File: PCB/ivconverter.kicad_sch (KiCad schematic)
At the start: 9 parts, among them U3 OPA1612AxD

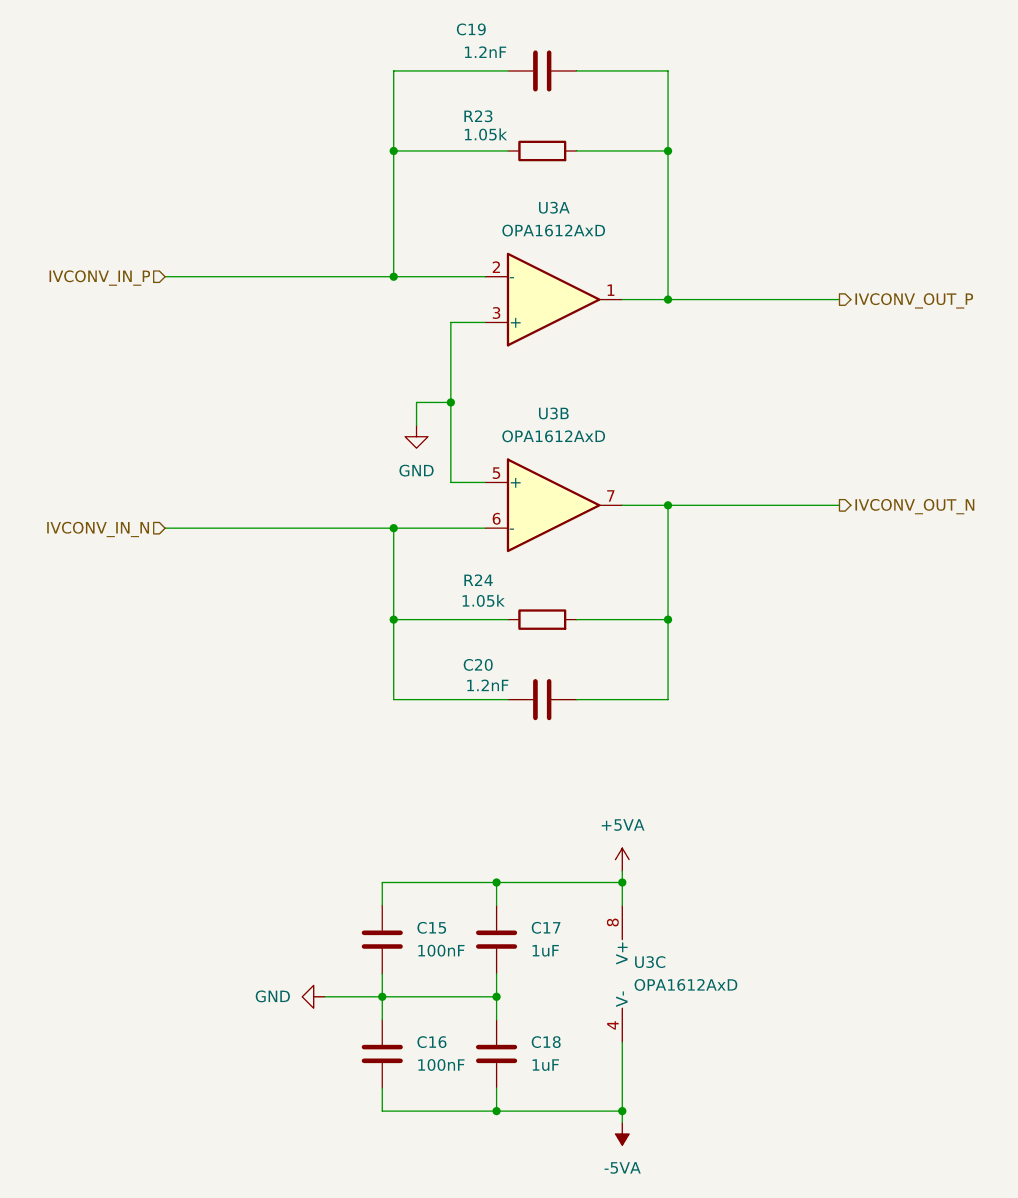
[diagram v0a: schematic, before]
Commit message: Changed single ended connector for gold plated part and changed resistor and capacitor values of opa1622 amp for improved power on high impedance headphones
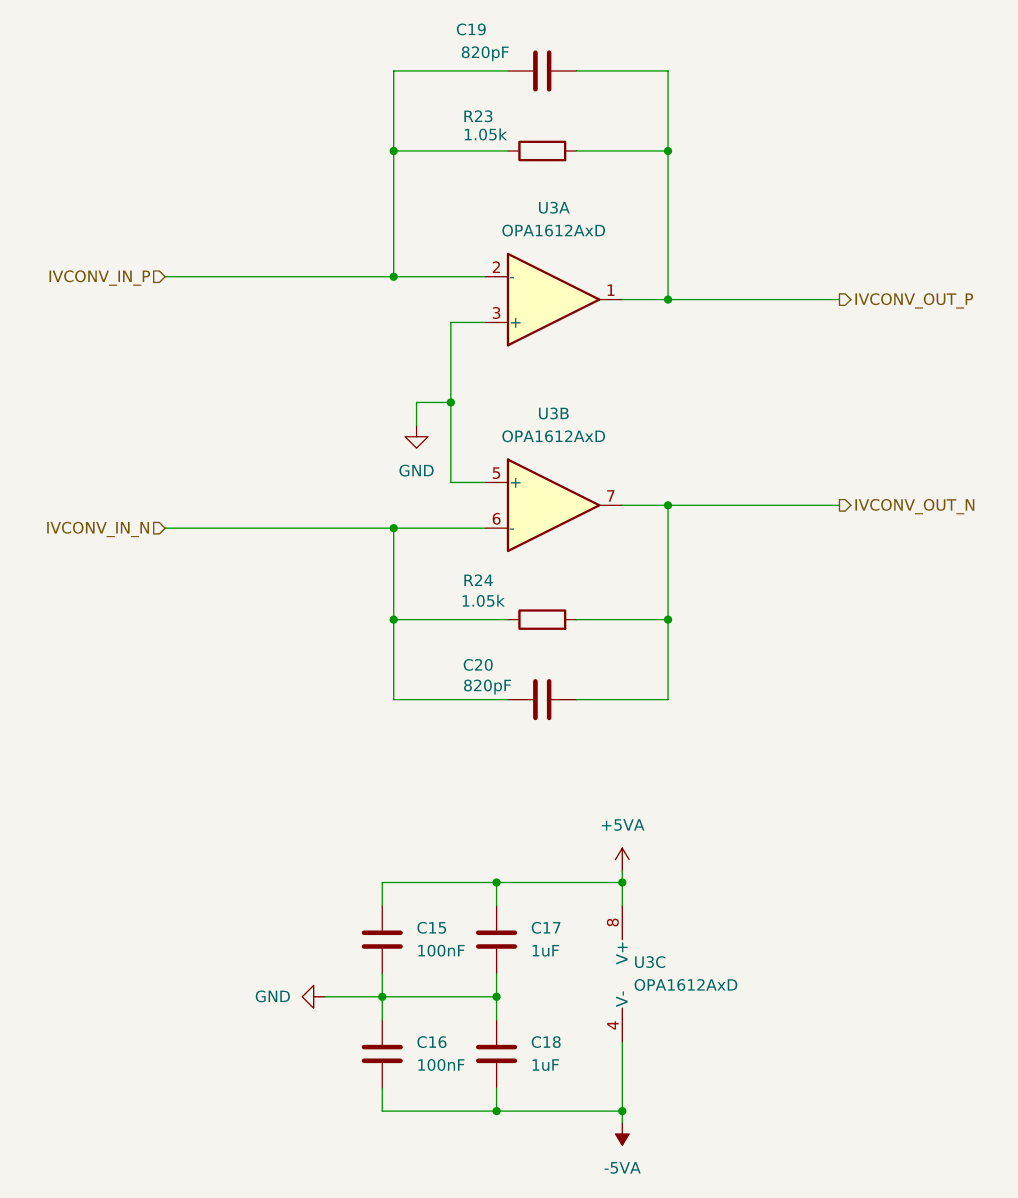
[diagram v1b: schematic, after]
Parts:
- C19, C20: value 1.2nF -> 820pF; JLCPCB Part # C576816 -> C99081
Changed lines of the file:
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@@
 			)
 		)
-		(property "Value" "1.2nF"
+		(property "Value" "820pF"
 			(at 143.764 115.316 90)
 			(effects
@@
 			)
 		)
-		(property "JLCPCB Part #" "C576816"
+		(property "JLCPCB Part #" "C99081"
 			(at 149.86 116.84 0)
 			(effects
@@
 			)
 		)
-		(property "Value" "1.2nF"
+		(property "Value" "820pF"
 			(at 143.51 44.958 90)
 			(effects
@@
 			)
 		)
-		(property "JLCPCB Part #" "C576816"
+		(property "JLCPCB Part #" "C99081"
 			(at 149.86 46.99 0)
 			(effects
